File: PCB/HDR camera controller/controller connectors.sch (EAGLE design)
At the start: 8 parts

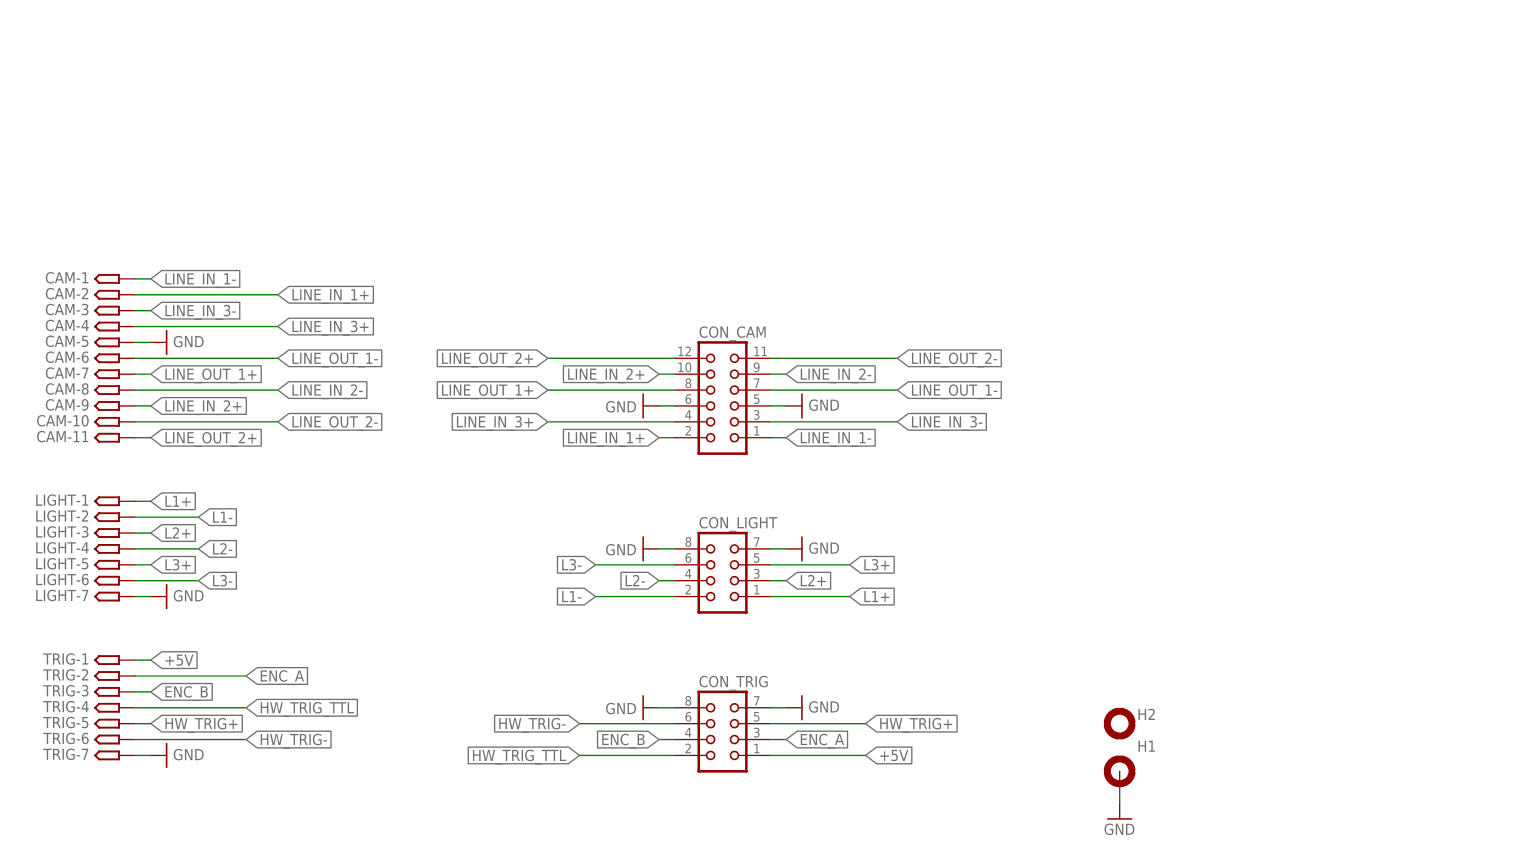
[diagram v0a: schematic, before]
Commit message: EEPROM implemented and tested, PCB docs
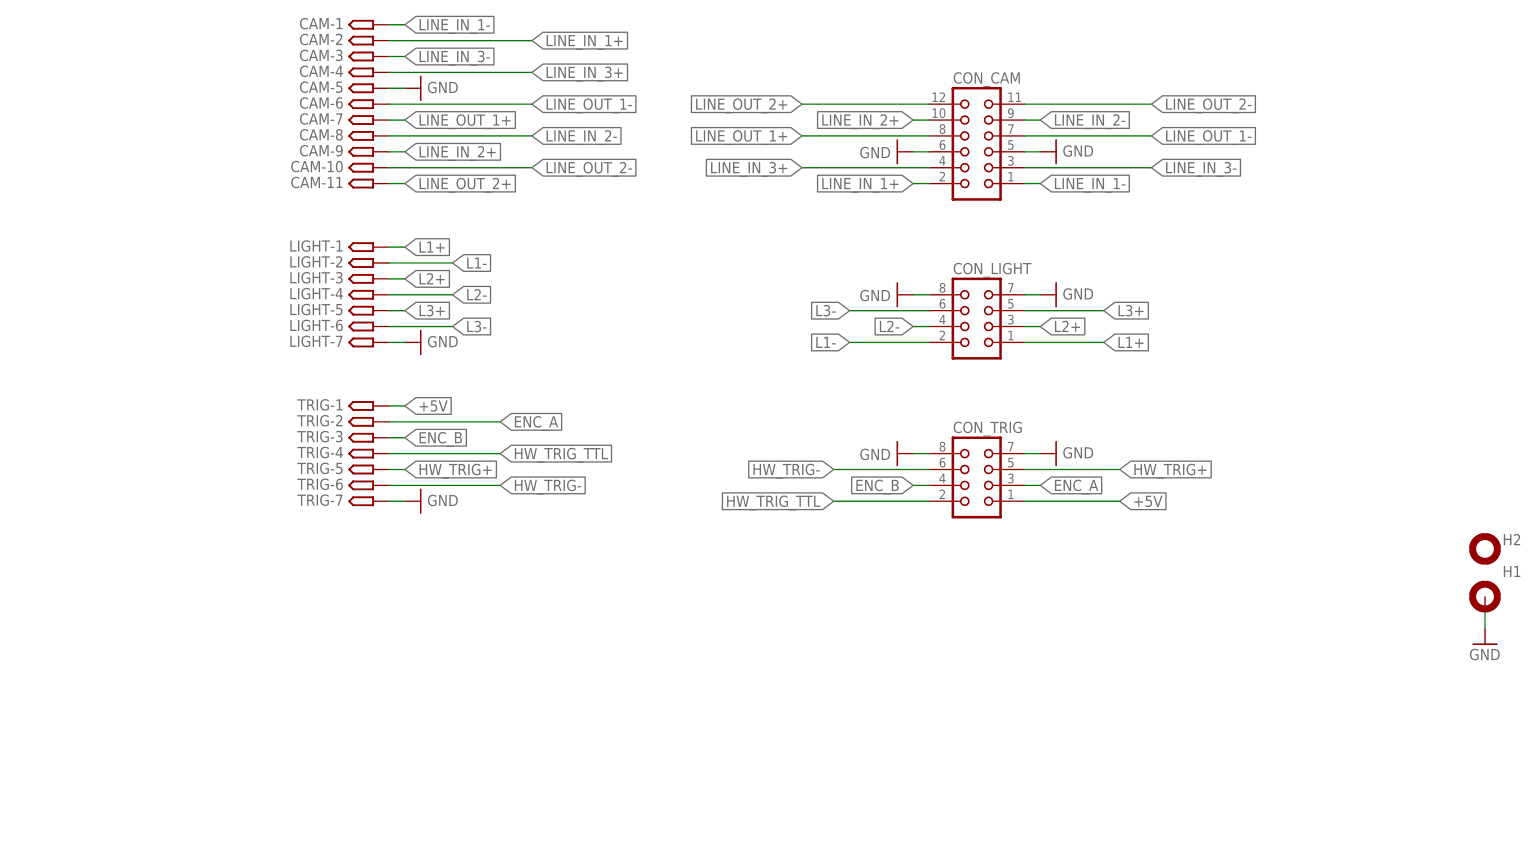
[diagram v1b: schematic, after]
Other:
- note removed: "I/O connectors"
- moved on the sheet: CAM-1, CAM-10, CAM-11, CAM-2, CAM-3, CAM-4, CAM-5, CAM-6, CAM-7, CAM-8, CAM-9, CON_CAM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
